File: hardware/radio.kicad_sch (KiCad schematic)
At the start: 16 parts, among them U7 nRF24L01P, U8 NRF24L01_Breakout, Y1 16MHz (C13738)

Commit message: feat(kicad): Cleared ERC errors and assigned footprints for all parts
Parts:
- C28, C29, C30, C31, C32, C33, C34, C35, C36: footprint (none) -> Capacitor_SMD:C_0402_1005Metric
- L1, L2, L3: footprint (none) -> Inductor_SMD:L_0402_1005Metric
- R20: footprint (none) -> Resistor_SMD:R_0402_1005Metric
- Y1: footprint (none) -> Crystal:Crystal_SMD_3225-4Pin_3.2x2.5mm
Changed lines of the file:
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@@
 			)
 		)
-		(property "Footprint" ""
+		(property "Footprint" "Capacitor_SMD:C_0402_1005Metric"
 			(at 196.5452 49.53 0)
 			(hide yes)
@@
 			)
 		)
-		(property "Footprint" ""
+		(property "Footprint" "Capacitor_SMD:C_0402_1005Metric"
 			(at 194.6148 57.15 0)
 			(hide yes)
@@
 			)
 		)
-		(property "Footprint" ""
+		(property "Footprint" "Inductor_SMD:L_0402_1005Metric"
 			(at 173.99 49.53 0)
 			(hide yes)
@@
 			)
 		)
-		(property "Footprint" ""
+		(property "Footprint" "Capacitor_SMD:C_0402_1005Metric"
 			(at 134.9248 35.56 0)
 			(hide yes)
@@
 			)
 		)
-		(property "Footprint" ""
+		(property "Footprint" "Capacitor_SMD:C_0402_1005Metric"
 			(at 190.1952 49.53 0)
 			(hide yes)
@@
 			)
 		)
-		(property "Footprint" ""
+		(property "Footprint" "Resistor_SMD:R_0402_1005Metric"
 			(at 112.522 82.55 90)
 			(hide yes)
@@
 			)
 		)
-		(property "Footprint" ""
+		(property "Footprint" "Capacitor_SMD:C_0402_1005Metric"
 			(at 189.23 56.1848 0)
 			(hide yes)
@@
 			)
 		)
-		(property "Footprint" ""
+		(property "Footprint" "Capacitor_SMD:C_0402_1005Metric"
 			(at 164.1348 93.98 0)
 			(hide yes)
@@
 			)
 		)
-		(property "Footprint" ""
+		(property "Footprint" "Capacitor_SMD:C_0402_1005Metric"
 			(at 128.5748 35.56 0)
 			(hide yes)
@@
 			)
 		)
-		(property "Footprint" ""
+		(property "Footprint" "Crystal:Crystal_SMD_3225-4Pin_3.2x2.5mm"
 			(at 172.72 86.36 0)
 			(hide yes)
@@
 			)
 		)
-		(property "Footprint" ""
+		(property "Footprint" "Capacitor_SMD:C_0402_1005Metric"
 			(at 182.5752 93.98 0)
 			(hide yes)
@@
 			)
 		)
-		(property "Footprint" ""
+		(property "Footprint" "Inductor_SMD:L_0402_1005Metric"
 			(at 173.99 57.15 0)
 			(hide yes)
@@
 			)
 		)
-		(property "Footprint" ""
+		(property "Footprint" "Inductor_SMD:L_0402_1005Metric"
 			(at 166.37 53.34 0)
 			(hide yes)
@@
 			)
 		)
-		(property "Footprint" ""
+		(property "Footprint" "Capacitor_SMD:C_0402_1005Metric"
 			(at 126.0348 86.36 0)
 			(hide yes)

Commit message: feat(kicad): Added radio application notes
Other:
- note added: "Application Notes 1)The traces from ANT1 and ANT2 through the matching network to the final output must be as short and straight as physically possible. No sharp 90-degree corners-use 45-degree bends or gentle curves. 2)The final trace leading out from the matching network to the antenna must maintain a strict 50-ohm characteristic impedance 3)No signal/ power traces should be routed underneath t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"
- moved on the sheet: U8
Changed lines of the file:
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@@
+		)
+	)
+	(text "Application Notes\n1)The traces from ANT1 and ANT2 through the matching network to the final output must be as short and straight as physically possible. No sharp 90-degree corners-use 45-degree bends or gentle curves.\n2)The final trace leading out from the matching network to the antenna must maintain a strict 50-ohm characteristic impedance\n3)No signal/ power traces should be routed underneath the RF section.\n4) Keep out zone should be used for the chip antenna"
+		(exclude_from_sim no)
+		(at 37.846 146.304 0)
+		(effects
+			(font
+				(size 1.27 1.27)
+			)
+			(justify left)
 		)
 	)
@@
 		(pts
 			(xy 148.59 80.01) (xy 146.05 80.01)
+		)
+		(stroke
+			(width 0)
+			(type default)
+		)
+	)
+	(wire
+		(pts
+			(xy 140.97 102.87) (xy 147.32 102.87)
 		)
 		(stroke
@@
 	(hierarchical_label "RADIO_ALT_CE"
 		(shape input)
-		(at 133.35 133.35 180)
+		(at 134.62 123.19 180)
 		(effects
 			(font
@@
 	(hierarchical_label "SPI3_MOSI"
 		(shape input)
-		(at 133.35 120.65 180)
+		(at 134.62 110.49 180)
 		(effects
 			(font
@@
 	(hierarchical_label "RADIO_ALT_INT"
 		(shape output)
-		(at 133.35 135.89 180)
+		(at 134.62 125.73 180)
 		(effects
 			(font
@@
 	(hierarchical_label "RADIO_ALT_CS"
 		(shape input)
-		(at 133.35 128.27 180)
+		(at 134.62 118.11 180)
 		(effects
 			(font
@@
 	(hierarchical_label "SPI3_MISO"
 		(shape output)
-		(at 133.35 123.19 180)
+		(at 134.62 113.03 180)
 		(effects
 			(font
@@
 	(hierarchical_label "SPI3_SCK"
 		(shape input)
-		(at 133.35 125.73 180)
+		(at 134.62 115.57 180)
 		(effects
 			(font
@@
 		(in_pos_files yes)
 		(dnp no)
-		(fields_autoplaced yes)
 		(property "Reference" "#PWR048"
 			(at 195.58 55.88 0)
@@
 		)
 		(property "Value" "GND"
-			(at 195.58 54.61 0)
+			(at 199.39 51.816 0)
 			(show_name no)
 			(do_not_autoplace no)
@@
 	(symbol
 		(lib_id "power:GND")
-		(at 146.05 143.51 0)
+		(at 147.32 133.35 0)
 		(unit 1)
 		(body_style 1)
@@
 		(fields_autoplaced yes)
 		(property "Reference" "#PWR045"
-			(at 146.05 149.86 0)
+			(at 147.32 139.7 0)
 			(hide yes)
 			(show_name no)
@@
 		)
 		(property "Value" "GND"
-			(at 146.05 148.59 0)
+			(at 147.32 138.43 0)
 			(show_name no)
 			(do_not_autoplace no)
@@
 		)
 		(property "Footprint" ""
-			(at 146.05 143.51 0)
+			(at 147.32 133.35 0)
 			(hide yes)
 			(show_name no)
@@
 		)
 		(property "Datasheet" ""
-			(at 146.05 143.51 0)
+			(at 147.32 133.35 0)
 			(hide yes)
 			(show_name no)
@@
 		)
 		(property "Description" "Power symbol creates a global label with name \"GND\" , ground"
-			(at 146.05 143.51 0)
+			(at 147.32 133.35 0)
 			(hide yes)
 			(show_name no)
@@
 	(symbol
 		(lib_id "RF:NRF24L01_Breakout")
-		(at 146.05 128.27 0)
+		(at 147.32 118.11 0)
 		(unit 1)
 		(body_style 1)
@@
 		(fields_autoplaced yes)
 		(property "Reference" "U8"
-			(at 156.21 126.9999 0)
+			(at 157.48 116.8399 0)
 			(show_name no)
 			(do_not_autoplace no)
@@
 		)
 		(property "Value" "NRF24L01_Breakout"
-			(at 156.21 129.5399 0)
+			(at 157.48 119.3799 0)
 			(show_name no)
 			(do_not_autoplace no)
@@
 		)
 		(property "Footprint" "RF_Module:nRF24L01_Breakout"
-			(at 149.86 113.03 0)
+			(at 151.13 102.87 0)
 			(hide yes)
 			(show_name no)
@@
 		)
 		(property "Datasheet" "http://www.nordicsemi.com/eng/content/download/2730/34105/file/nRF24L01_Product_Specification_v2_0.pdf"
-			(at 146.05 130.81 0)
+			(at 147.32 120.65 0)
 			(hide yes)
 			(show_name no)
@@
 		)
 		(property "Description" "Ultra low power 2.4GHz RF Transceiver, Carrier PCB"
-			(at 146.05 128.27 0)
+			(at 147.32 118.11 0)
 			(hide yes)
 			(show_name no)
@@
 	(symbol
 		(lib_id "power:+3V3")
-		(at 146.05 113.03 0)
+		(at 140.97 102.87 0)
 		(unit 1)
 		(body_style 1)
@@
 		(in_pos_files yes)
 		(dnp no)
-		(fields_autoplaced yes)
 		(property "Reference" "#PWR044"
-			(at 146.05 116.84 0)
+			(at 140.97 106.68 0)
 			(hide yes)
 			(show_name no)
@@
 		)
 		(property "Value" "+3V3"
-			(at 146.05 107.95 0)
+			(at 143.764 101.6 0)
 			(show_name no)
 			(do_not_autoplace no)
@@
 		)
 		(property "Footprint" ""
-			(at 146.05 113.03 0)
+			(at 140.97 102.87 0)
 			(hide yes)
 			(show_name no)
@@
 		)
 		(property "Datasheet" ""
-			(at 146.05 113.03 0)
+			(at 140.97 102.87 0)
 			(hide yes)
 			(show_name no)
@@
 		)
 		(property "Description" "Power symbol creates a global label with name \"+3V3\""
-			(at 146.05 113.03 0)
-			(hide yes)
-			(show_name no)
+			(at 140.97 102.87 0)
+			(hide yes)
+			(show_name no)

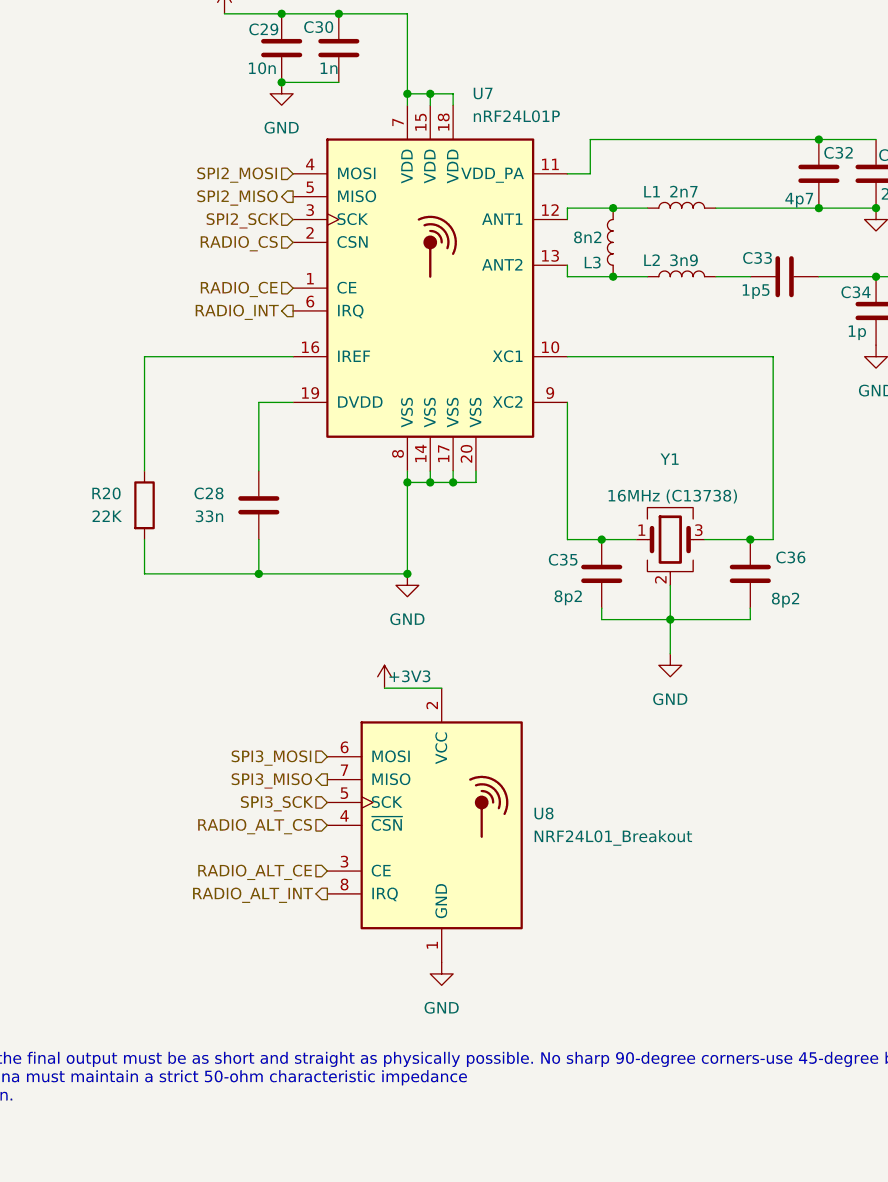
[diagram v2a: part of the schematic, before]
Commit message: feat(kicad): Updated schematic to keep traces shorter on the layout Restarting layout
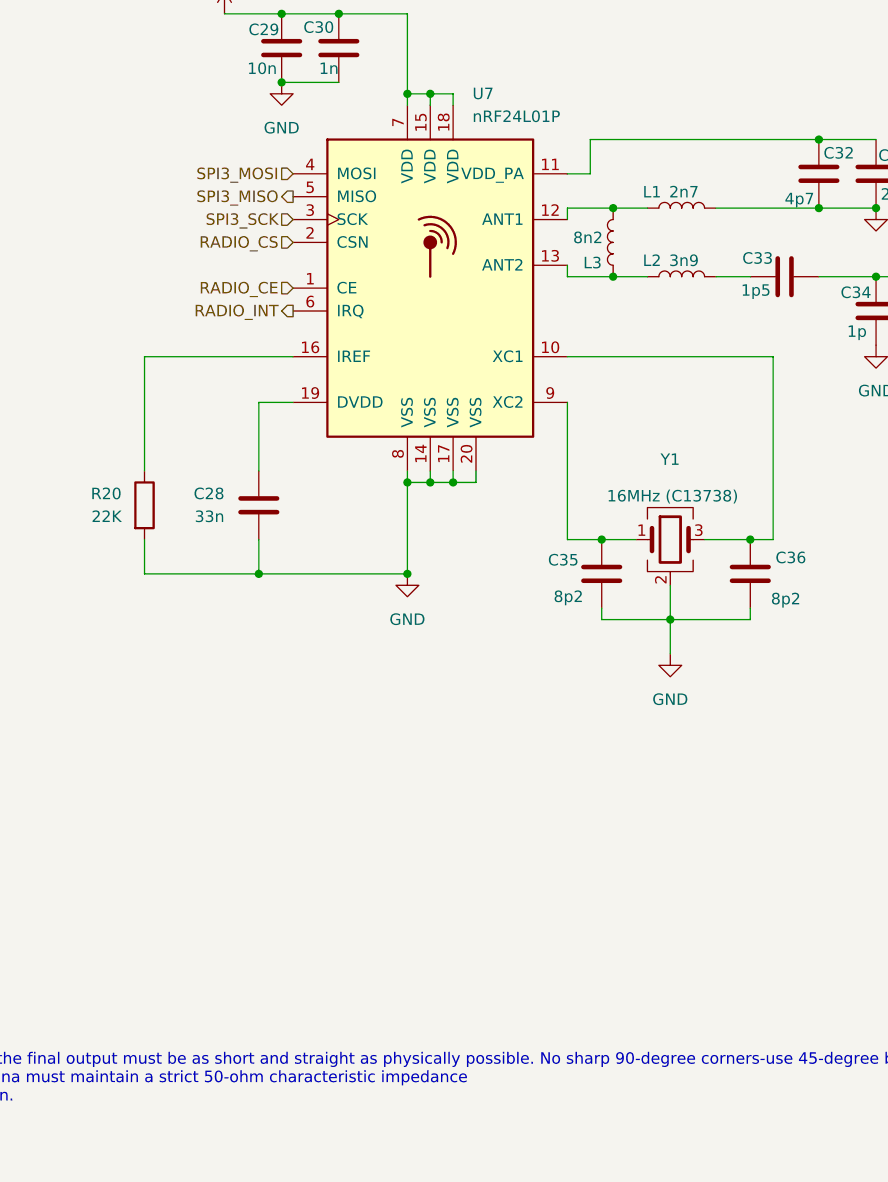
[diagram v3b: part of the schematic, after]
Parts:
- removed U8: NRF24L01_Breakout, RF_Module:nRF24L01_Breakout, symbol RF:NRF24L01_Breakout
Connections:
- net SPI2_MISO is gone; now on net SPI3_MISO: U7.5 (MISO)
- net SPI2_MOSI is gone; now on net SPI3_MOSI: U7.4 (MOSI)
- net SPI2_SCK is gone; now on net SPI3_SCK: U7.3 (SCK)

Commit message: feat(kicad): Updated traces to reduce power plane slotting Finished inital pass of the NRF layout
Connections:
- net VDD_PA: now reaches C31.1, C32.1, U7.11 (VDD_PA)
- net ANT1: now reaches L1.1, L3.2, U7.12 (ANT1)
- net ANT2: now reaches L2.1, L3.1, U7.13 (ANT2)
- net DVDD: now reaches C28.1, U7.19 (DVDD)
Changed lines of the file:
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@@
+		)
+	)
+	(label "ANT1"
+		(at 161.29 49.53 0)
+		(effects
+			(font
+				(size 1.27 1.27)
+			)
+			(justify left bottom)
+		)
+	)
+	(label "VDD_PA"
+		(at 163.83 41.91 0)
+		(effects
+			(font
+				(size 1.27 1.27)
+			)
+			(justify left bottom)
+		)
+	)
+	(label "DVDD"
+		(at 129.54 71.12 180)
+		(effects
+			(font
+				(size 1.27 1.27)
+			)
+			(justify right bottom)
 		)
 	)
@@
 		(effects
 			(font
+				(size 1.27 1.27)
+			)
+			(justify left bottom)
+		)
+	)
+	(label "ANT2"
+		(at 161.29 57.15 0)
+		(effects
+			(font

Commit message: feat(kicad): Added chip antenna footprint Still deciding between chip vs trace
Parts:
- added ANT1: ANT016008LCS2442MA1, ANT016008LCS2442MA1:ANT_ANT016008LCS2442MA1, symbol ANT016008LCS2442MA1:ANT016008LCS2442MA1
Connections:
- net 50ohm: now also ANT1.4 (FEEDING)
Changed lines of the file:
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@@
-	(wire
-		(pts
-			(xy 214.63 57.15) (xy 195.58 57.15)
-		)
-		(stroke
-			(width 0)
-			(type default)
-		)
-	)
 	(wire
 		(pts
@@
 		(pts
 			(xy 146.05 36.83) (xy 148.59 36.83)
+		)
+		(stroke
+			(width 0)
+			(type default)
+		)
+	)
+	(wire
+		(pts
+			(xy 195.58 57.15) (xy 204.47 57.15)
 		)
 		(stroke
@@
 	)
 	(label "50ohm"
-		(at 214.63 57.15 0)
+		(at 195.58 57.15 0)
 		(effects
 			(font
@@
 					(unit 1)
 				)
+			)
+		)
+	)
+	(symbol
+		(lib_id "ANT016008LCS2442MA1:ANT016008LCS2442MA1")
+		(at 222.25 59.69 0)
+		(unit 1)
+		(body_style 1)
+		(exclude_from_sim no)
+		(in_bom yes)
+		(on_board yes)
+		(in_pos_files yes)
+		(dnp no)
+		(fields_autoplaced yes)
+		(property "Reference" "ANT1"
+			(at 238.76 58.4199 0)
+			(show_name no)
+			(do_not_autoplace no)
+			(effects
+				(font
+					(size 1.27 1.27)
+				)
+				(justify left)
+			)
+		)
+		(property "Value" "ANT016008LCS2442MA1"
+			(at 238.76 60.9599 0)
+			(show_name no)
+			(do_not_autoplace no)
+			(effects
+				(font
+					(size 1.27 1.27)
+				)
+				(justify left)
+			)
+		)
+		(property "Footprint" "ANT016008LCS2442MA1:ANT_ANT016008LCS2442MA1"
+			(at 222.25 59.69 0)
+			(hide yes)
+			(show_name no)
+			(do_not_autoplace no)
+			(effects
+				(font
+					(size 1.27 1.27)
+				)
+				(justify bottom)
+			)
+		)
+		(property "Datasheet" ""
+			(at 222.25 59.69 0)
+			(hide yes)
+			(show_name no)
+			(do_not_autoplace no)
+			(effects
+				(font
+					(size 1.27 1.27)
+				)
+			)
+		)
+		(property "Description" ""
+			(at 222.25 59.69 0)
+			(hide yes)
+			(show_name no)
+			(do_not_autoplace no)
+			(effects
+				(font
+					(size 1.27 1.27)
+				)
+			)
+		)
+		(property "PARTREV" "sep 2016"
+			(at 222.25 59.69 0)
+			(hide yes)
+			(show_name no)
+			(do_not_autoplace no)
+			(effects
+				(font
+					(size 1.27 1.27)
+				)
+				(justify bottom)
+			)
+		)
+		(property "STANDARD" "Manufacturer Recommendations"
+			(at 222.25 59.69 0)
+			(hide yes)
+			(show_name no)
+			(do_not_autoplace no)
+			(effects
+				(font
+					(size 1.27 1.27)
+				)
+				(justify bottom)
+			)
+		)
+		(property "MAXIMUM_PACKAGE_HEIGHT" "0.4mm"
+			(at 222.25 59.69 0)
+			(hide yes)
+			(show_name no)
+			(do_not_autoplace no)
+			(effects
+				(font
+					(size 1.27 1.27)
+				)
+				(justify bottom)
+			)
+		)
+		(property "MANUFACTURER" "TDK"
+			(at 222.25 59.69 0)
+			(hide yes)
+			(show_name no)
+			(do_not_autoplace no)
+			(effects
+				(font
+					(size 1.27 1.27)
+				)
+				(justify bottom)
+			)
+		)
+		(pin "1"
+		)
+		(pin "4"
+		)
+		(instances
+			(project "swarm_drone"
+				(path "/3a60ba80-6c79-4a64-bdfd-12960f1d2492/011e700c-c450-4362-bd4b-119060744e53"
+					(reference "ANT1")
+					(unit 1)
+				)

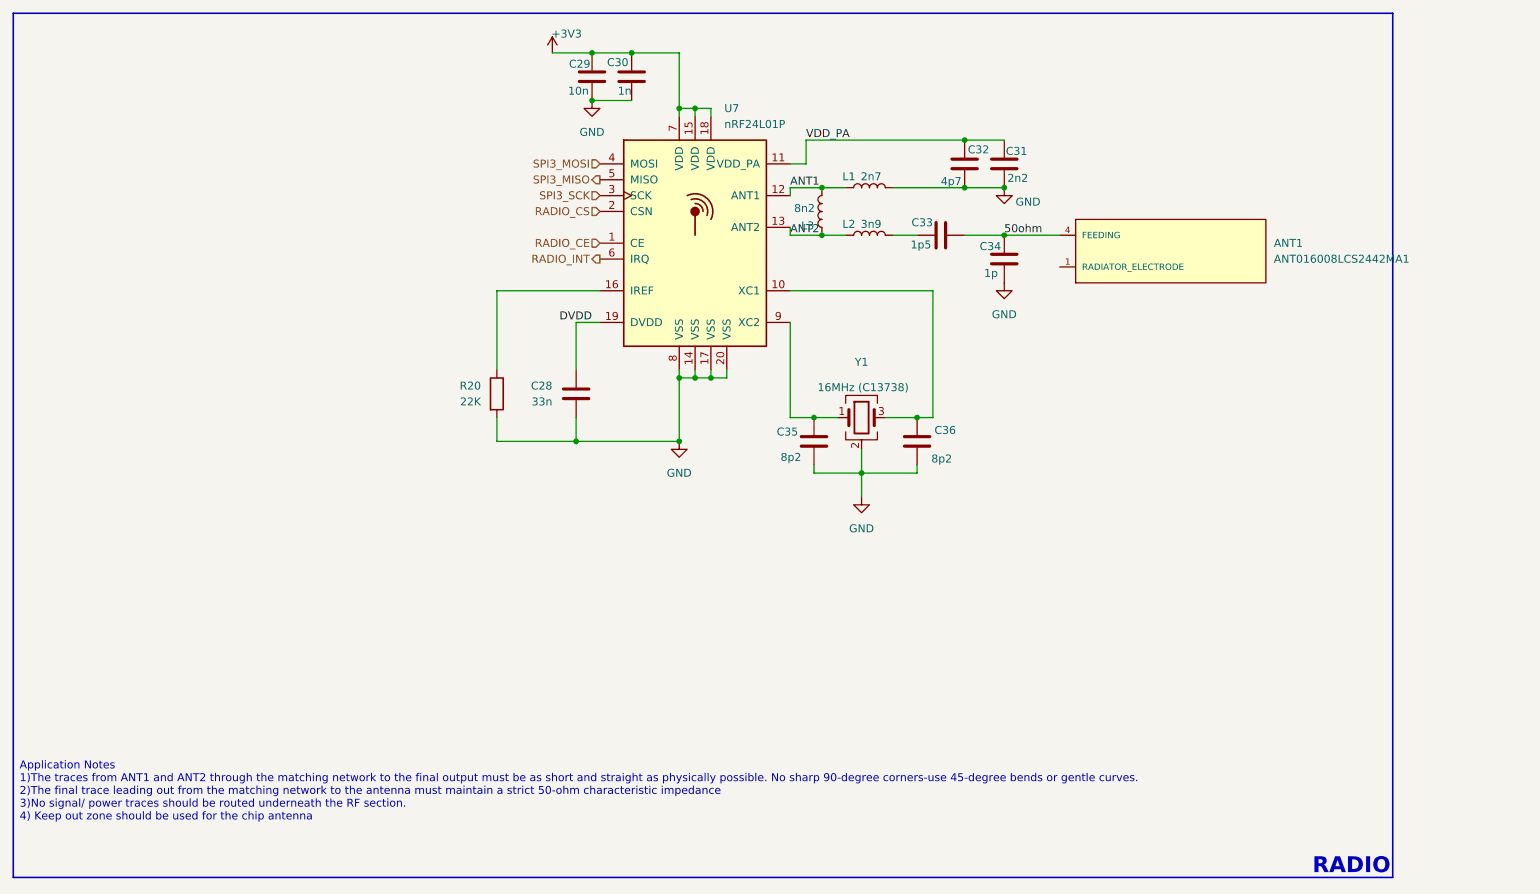
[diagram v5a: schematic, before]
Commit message: feat(kicad): After several revisions finished rf section and improved ground plane topology and signal distances
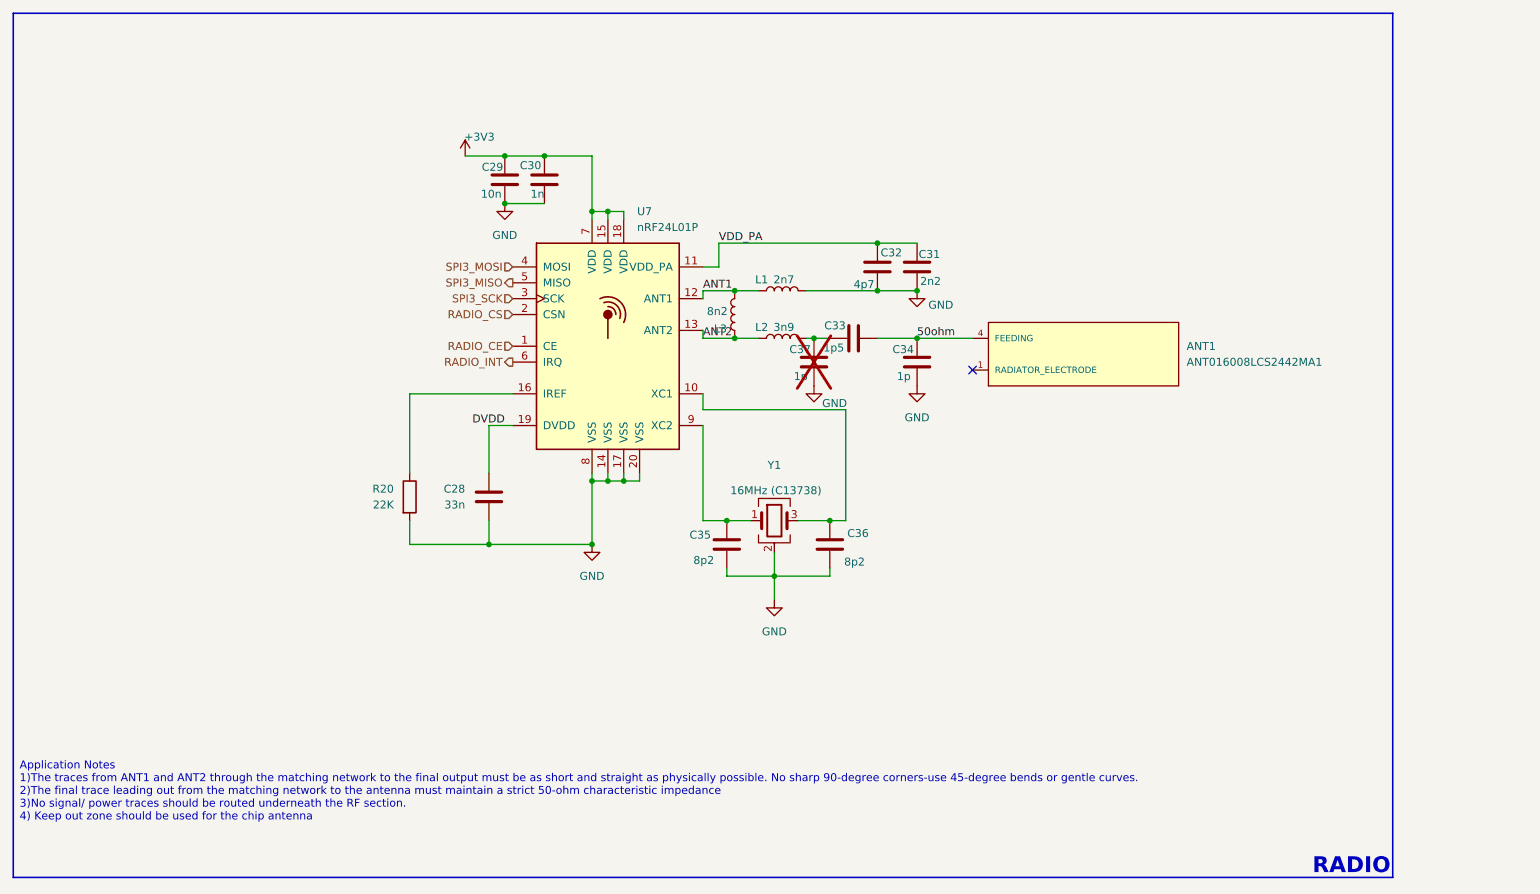
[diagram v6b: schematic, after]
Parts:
- added C37: 1p, Capacitor_SMD:C_0402_1005Metric, symbol Device:C
- ANT1: footprint ANT016008LCS2442MA1:ANT_ANT016008LCS2442MA1 -> Antenna:ANT_ANT016008LCS2442MA1
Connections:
- net GND: now also C37.1
- net at C33.1, L2.2: now also C37.2
- no-connect marks 0 -> 1
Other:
- moved on the sheet: ANT1, C28, C29, C30, C31, C32, C33, C34, C35, C36, L1, L2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

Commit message: feat(kicad): Routing complete, assigning jlc components to each footprint
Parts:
- ANT1: LCSC (none) -> C76585
- R20: LCSC (none) -> C25768
- U7: LCSC (none) -> C8791
- Y1: LCSC (none) -> C13738
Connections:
- net GND: no longer L1.2
- net VDD_PA: now also L1.2
